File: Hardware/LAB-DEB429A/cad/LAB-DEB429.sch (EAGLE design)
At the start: 102 parts, among them J1 TSW-132-02-S-D, J2 TSW-132-02-S-D, U1 LAB-ADSM300F, U10 SF-MICROSD, U11 25MPX, U12 LAB-PPS330D, U13 LAB-PPS330D, U14 LAB-PPS330D, U15 SI1143, U16 LAB-PPS330D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

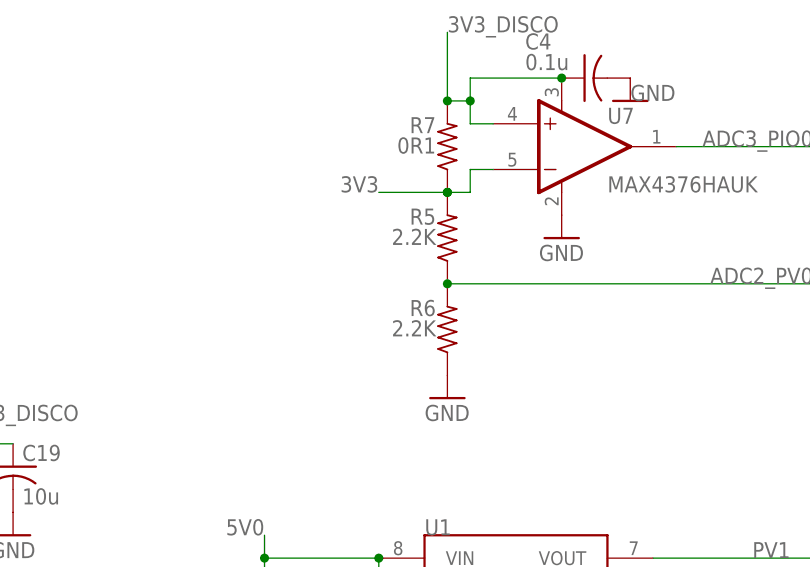
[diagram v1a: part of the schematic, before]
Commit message: 1) Synchronizing some of the reference designators on the BOM vs the schematic (capacitors specifically) 2) Removing the 50pos connector from the BOM -- its supposed to be 64 ... dumbass.
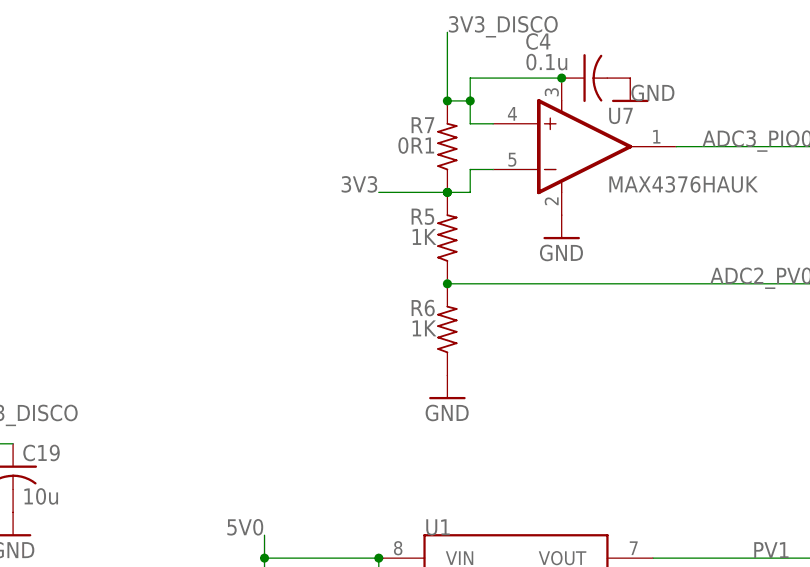
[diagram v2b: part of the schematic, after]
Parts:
- R5, R6: value 2.2K -> 1K
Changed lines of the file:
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@@
 <?xml version="1.0" encoding="utf-8"?>
 <!DOCTYPE eagle SYSTEM "eagle.dtd">
-<eagle version="7.3.0">
+<eagle version="6.6.0">
 <drawing>
 <settings>
@@
 <part name="R4" library="rcl" deviceset="R-US_" device="R0603" value="30"/>
 <part name="FRAME1" library="frames" deviceset="FRAME_B_L" device=""/>
-<part name="R5" library="rcl" deviceset="R-US_" device="R0603" value="2.2K"/>
-<part name="R6" library="rcl" deviceset="R-US_" device="R0603" value="2.2K"/>
+<part name="R5" library="rcl" deviceset="R-US_" device="R0603" value="1K"/>
+<part name="R6" library="rcl" deviceset="R-US_" device="R0603" value="1K"/>
 <part name="GND7" library="SparkFun-Aesthetics" deviceset="GND" device=""/>
 <part name="U7" library="PEGMA" deviceset="MAX4376" device="" value="MAX4376HAUK"/>

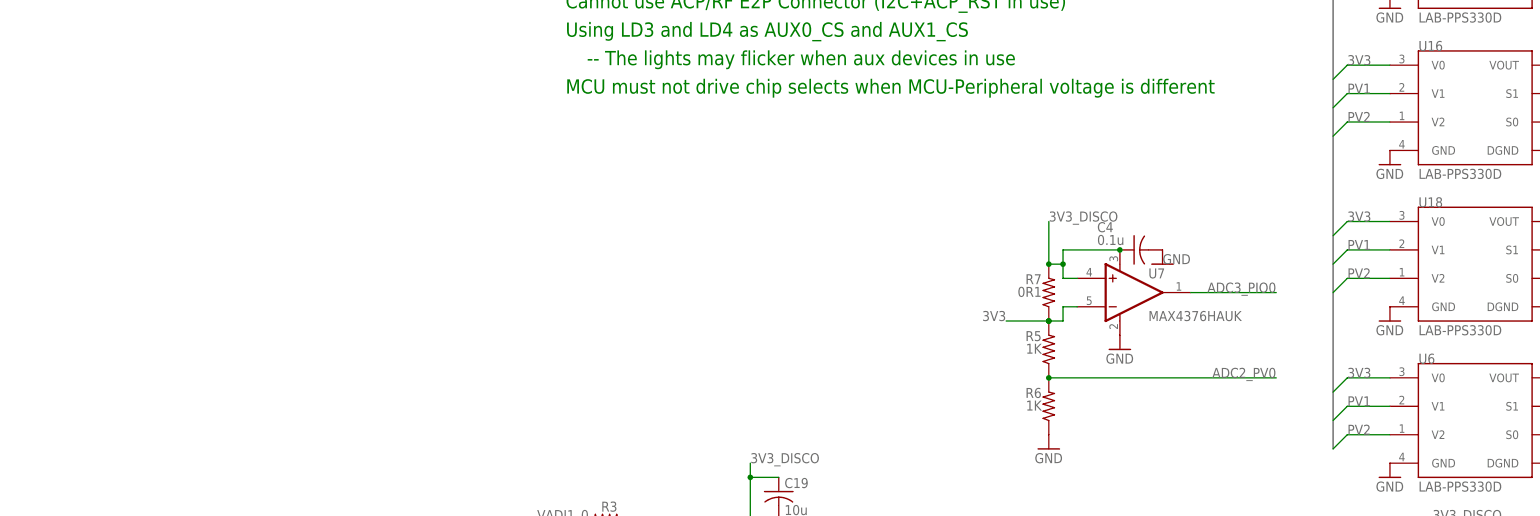
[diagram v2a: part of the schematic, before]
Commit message: 1) Updating the schematic with the latest notes from test.
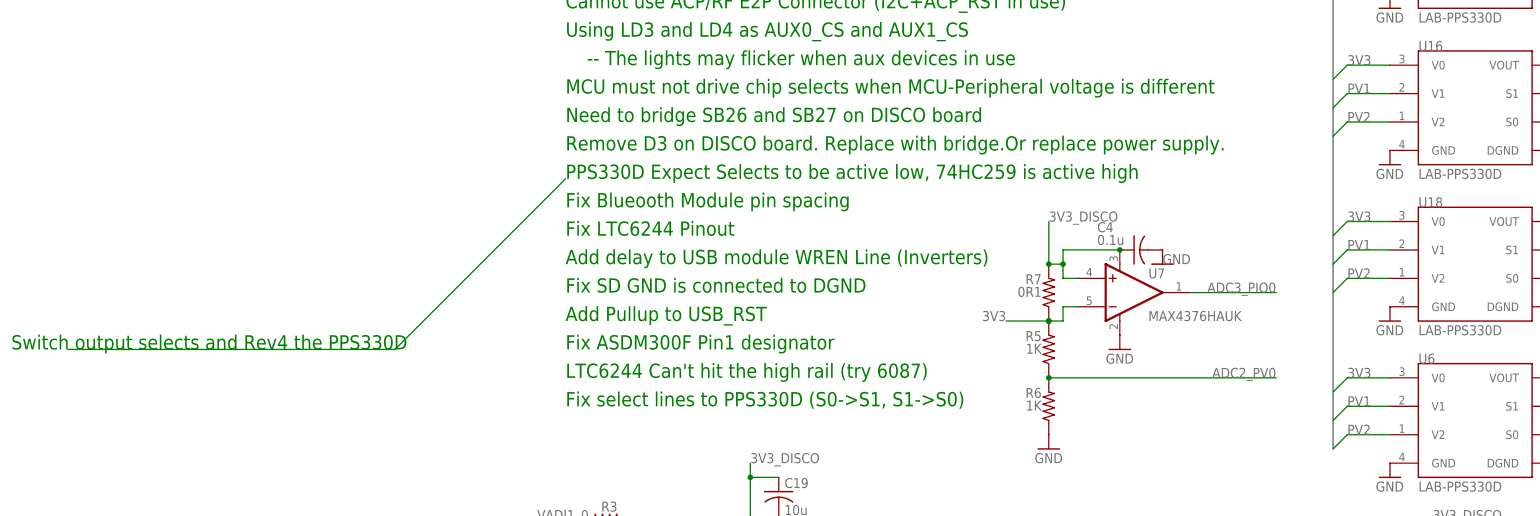
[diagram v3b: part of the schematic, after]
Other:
- note added: "Add Pullup to USB_RST"
- note added: "Add delay to USB module WREN Line (Inverters)"
- note added: "Fix ASDM300F Pin1 designator"
- note added: "Fix Blueooth Module pin spacing"
- note added: "Fix LTC6244 Pinout"
- note added: "Fix SD GND is connected to DGND"
- note added: "Fix select lines to PPS330D (S0->S1, S1->S0)"
- note added: "LTC6244 Can't hit the high rail (try 6087)"
- note added: "Need to bridge SB26 and SB27 on DISCO board"
- note added: "PPS330D Expect Selects to be active low, 74HC259 is active high"
- note added: "Remove D3 on DISCO board. Replace with bridge.Or replace power supply."
- note added: "Switch output selects and Rev4 the PPS330D"
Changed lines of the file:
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@@
 <text x="13.97" y="142.24" size="2.54" layer="91">-- The lights may flicker when aux devices in use</text>
 <text x="10.16" y="137.16" size="2.54" layer="91">MCU must not drive chip selects when MCU-Peripheral voltage is different</text>
+<text x="10.16" y="132.08" size="2.54" layer="91">Need to bridge SB26 and SB27 on DISCO board</text>
+<text x="10.16" y="127" size="2.54" layer="91">Remove D3 on DISCO board. Replace with bridge.Or replace power supply.</text>
+<text x="10.16" y="91.44" size="2.54" layer="91">Fix ASDM300F Pin1 designator</text>
+<text x="10.16" y="116.84" size="2.54" layer="91">Fix Blueooth Module pin spacing</text>
+<text x="10.16" y="111.76" size="2.54" layer="91">Fix LTC6244 Pinout</text>
+<text x="10.16" y="106.68" size="2.54" layer="91">Add delay to USB module WREN Line (Inverters)</text>
+<text x="10.16" y="101.6" size="2.54" layer="91">Fix SD GND is connected to DGND</text>
+<text x="10.16" y="96.52" size="2.54" layer="91">Add Pullup to USB_RST</text>
+<text x="10.16" y="121.92" size="2.54" layer="91">PPS330D Expect Selects to be active low, 74HC259 is active high</text>
+<text x="10.16" y="86.36" size="2.54" layer="91">LTC6244 Can't hit the high rail (try 6087)</text>
+<text x="10.16" y="81.28" size="2.54" layer="91">Fix select lines to PPS330D (S0-&gt;S1, S1-&gt;S0)</text>
+<text x="-88.9" y="91.44" size="2.54" layer="91">Switch output selects and Rev4 the PPS330D</text>
 </plain>
 <instances>
@@
 </segment>
 </net>
+<net name="N$43" class="0">
+<segment>
+<wire x1="10.16" y1="121.92" x2="-20.32" y2="91.44" width="0.1524" layer="91"/>
+<wire x1="-20.32" y1="91.44" x2="-78.74" y2="91.44" width="0.1524" layer="91"/>
+</segment>
+</net>

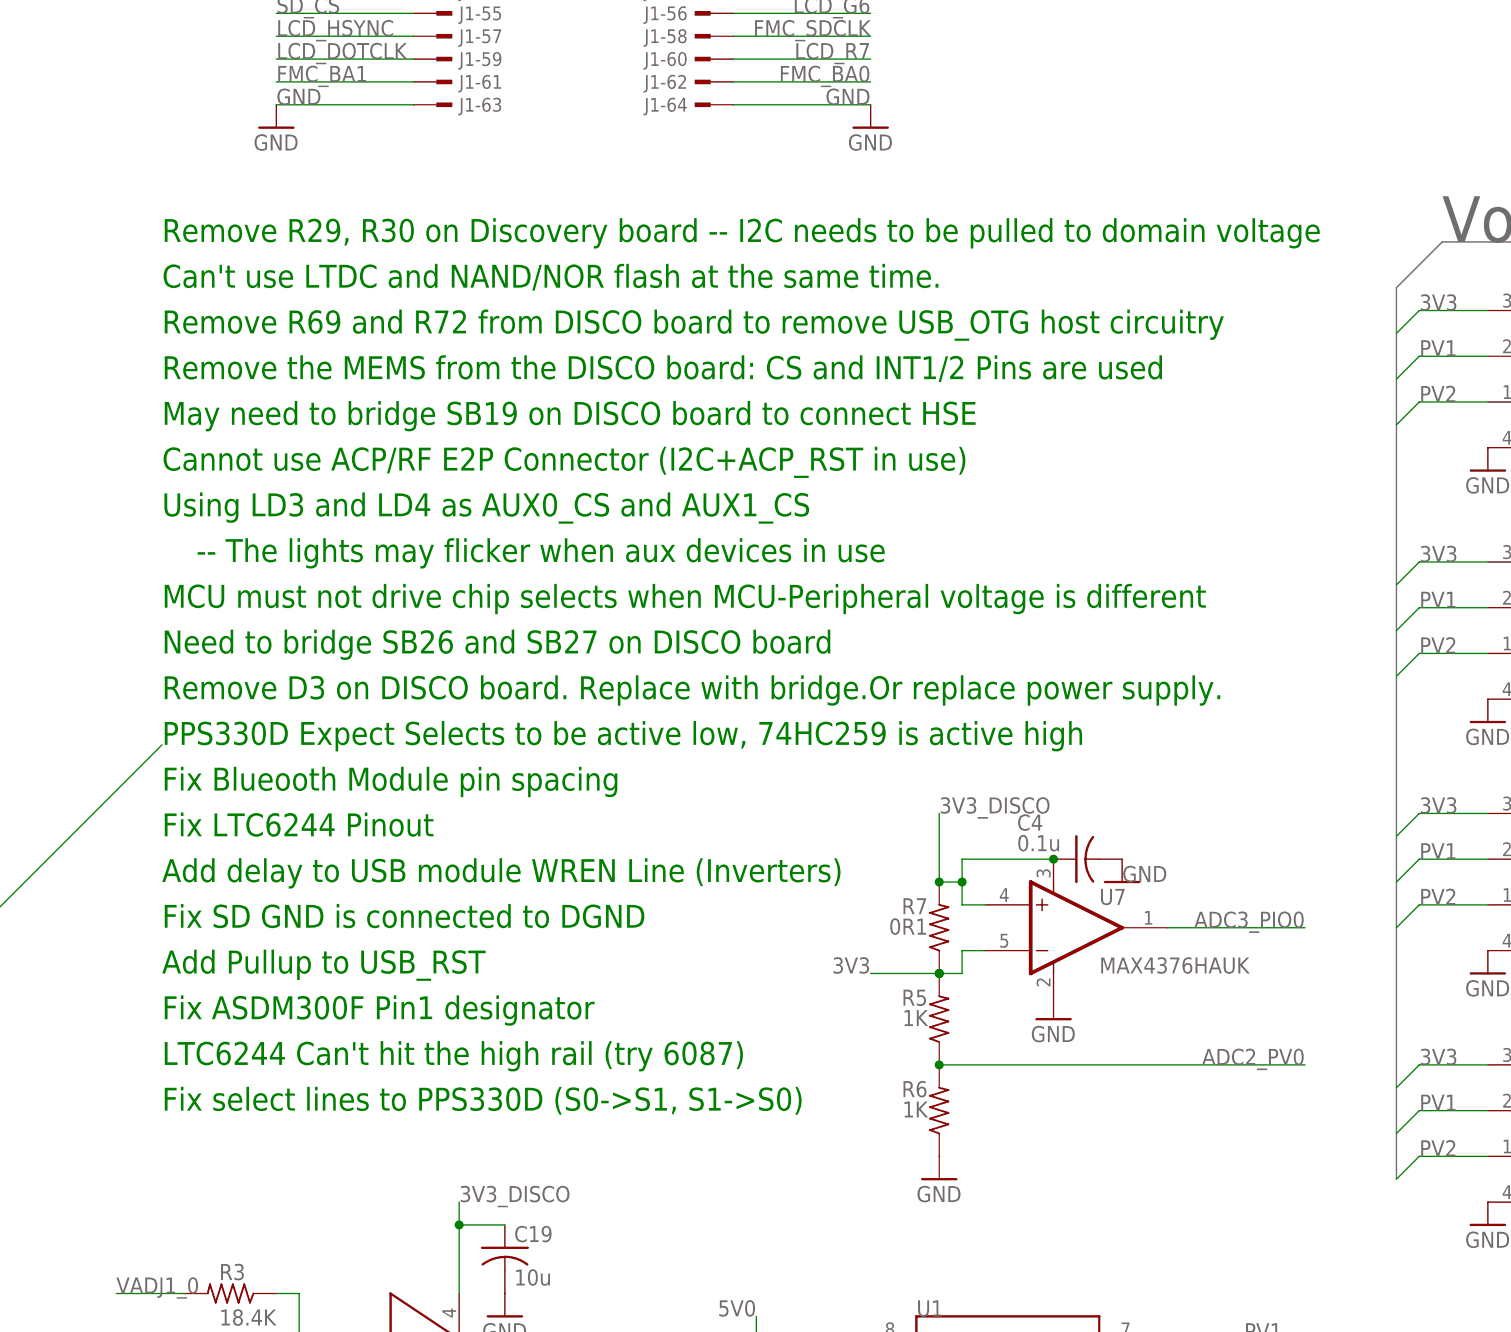
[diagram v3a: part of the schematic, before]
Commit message: 1) Comments about open collector chip selects
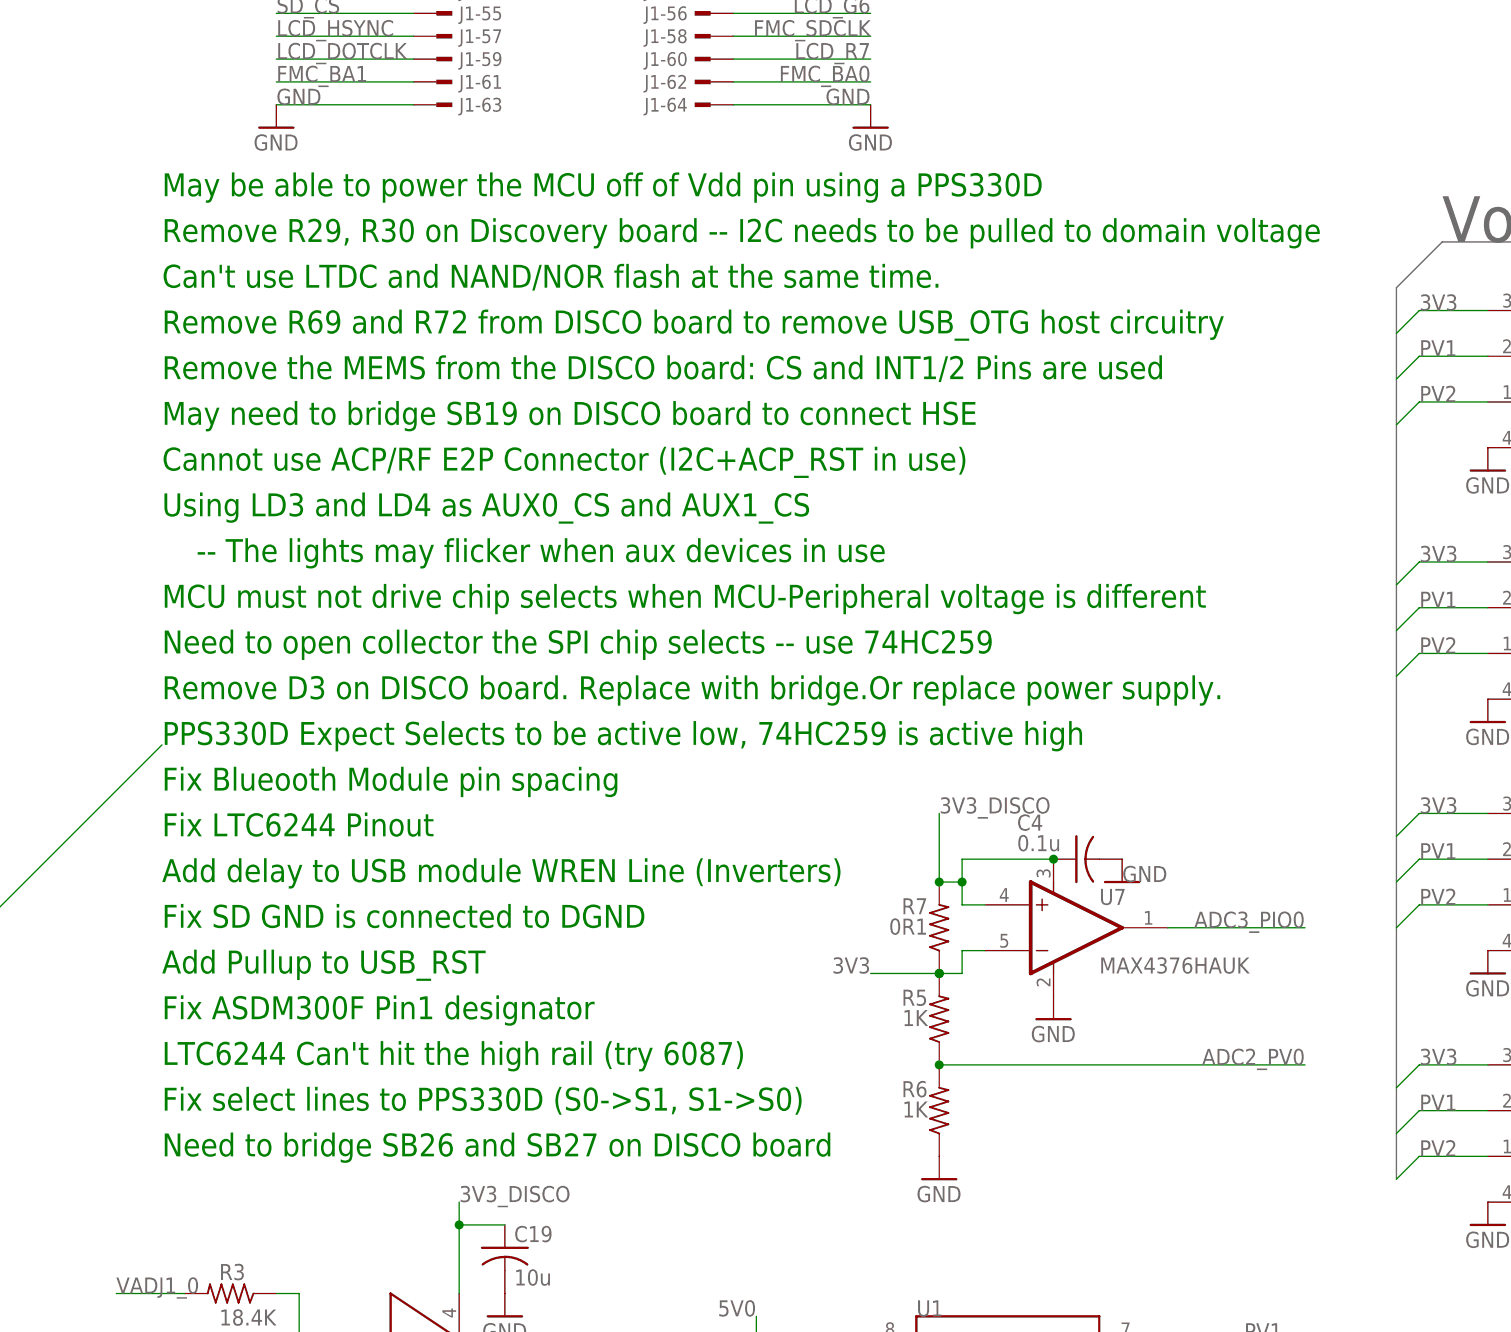
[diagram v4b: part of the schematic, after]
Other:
- note added: "May be able to power the MCU off of Vdd pin using a PPS330D"
- note added: "Need to open collector the SPI chip selects -- use 74HC259"
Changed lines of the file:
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@@
 <text x="13.97" y="142.24" size="2.54" layer="91">-- The lights may flicker when aux devices in use</text>
 <text x="10.16" y="137.16" size="2.54" layer="91">MCU must not drive chip selects when MCU-Peripheral voltage is different</text>
-<text x="10.16" y="132.08" size="2.54" layer="91">Need to bridge SB26 and SB27 on DISCO board</text>
+<text x="10.16" y="76.2" size="2.54" layer="91">Need to bridge SB26 and SB27 on DISCO board</text>
 <text x="10.16" y="127" size="2.54" layer="91">Remove D3 on DISCO board. Replace with bridge.Or replace power supply.</text>
 <text x="10.16" y="91.44" size="2.54" layer="91">Fix ASDM300F Pin1 designator</text>
@@
 <text x="10.16" y="81.28" size="2.54" layer="91">Fix select lines to PPS330D (S0-&gt;S1, S1-&gt;S0)</text>
 <text x="-88.9" y="91.44" size="2.54" layer="91">Switch output selects and Rev4 the PPS330D</text>
+<text x="10.16" y="132.08" size="2.54" layer="91">Need to open collector the SPI chip selects -- use 74HC259</text>
+<text x="10.16" y="182.88" size="2.54" layer="91">May be able to power the MCU off of Vdd pin using a PPS330D</text>
 </plain>
 <instances>

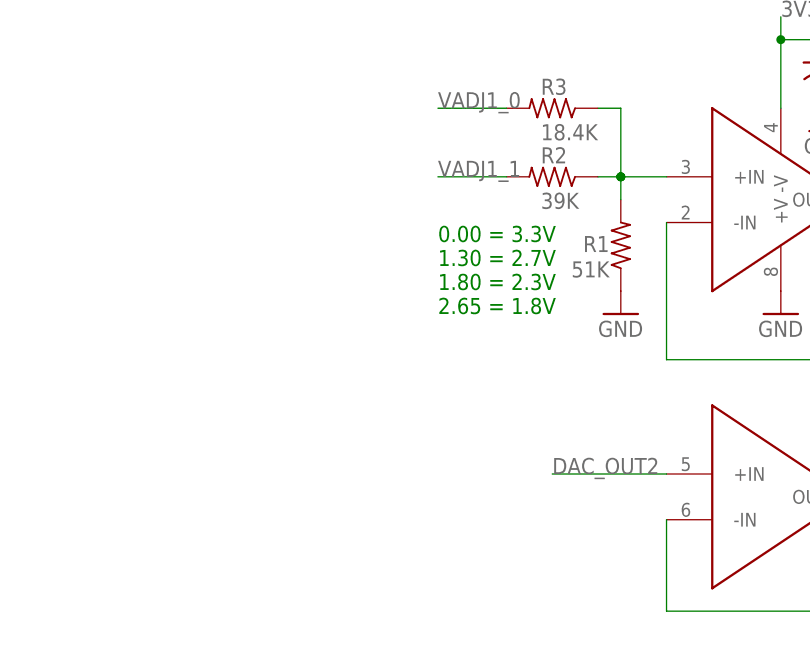
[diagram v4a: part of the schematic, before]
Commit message: 1) Updating some of the notes regarding power supply voltages on the schematic 2) Updates to the POST procedure for each voltage domain.
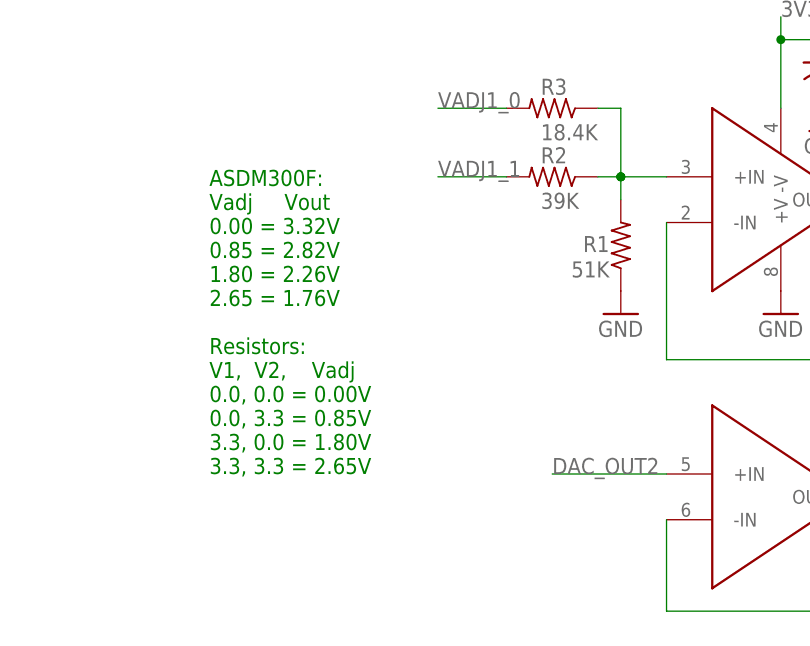
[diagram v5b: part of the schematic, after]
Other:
- note added: "ASDM300F: Vadj Vout 0.00 = 3.32V 0.85 = 2.82V 1.80 = 2.26V 2.65 = 1.76V Resistors: V1, V2, Vadj 0.0, 0.0 = 0.00V 0.0, 3.3 = 0.85V 3.3, 0.0 = 1.80V 3.3, 3.3 = 2.65V"
- note removed: "0.00 = 3.3V 1.30 = 2.7V 1.80 = 2.3V 2.65 = 1.8V"
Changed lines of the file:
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@@
 <text x="10.16" y="172.72" size="2.54" layer="91">Can't use LTDC and NAND/NOR flash at the same time.</text>
 <text x="10.16" y="167.64" size="2.54" layer="91">Remove R69 and R72 from DISCO board to remove USB_OTG host circuitry</text>
-<text x="5.08" y="38.1" size="1.778" layer="91">0.00 = 3.3V
-1.30 = 2.7V
-1.80 = 2.3V
-2.65 = 1.8V</text>
+<text x="-20.32" y="20.32" size="1.778" layer="91">ASDM300F:
+Vadj     Vout
+0.00 = 3.32V
+0.85 = 2.82V
+1.80 = 2.26V
+2.65 = 1.76V
+Resistors:
+V1,  V2,    Vadj
+0.0, 0.0 = 0.00V
+0.0, 3.3 = 0.85V
+3.3, 0.0 = 1.80V
+3.3, 3.3 = 2.65V</text>
 <text x="276.86" y="177.8" size="6.4516" layer="95" rot="MR0">IODVS Devices</text>
 <text x="152.4" y="177.8" size="5.08" layer="95">Voltage Bus</text>
